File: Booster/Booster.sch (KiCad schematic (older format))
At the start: 0 parts

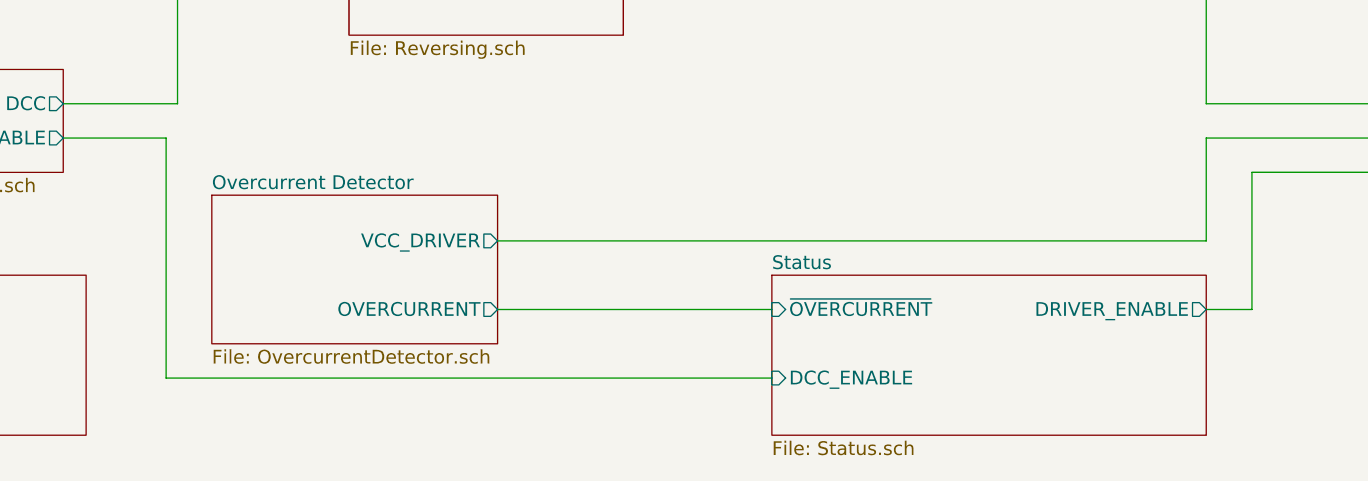
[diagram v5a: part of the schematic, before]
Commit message: Added 555 timer to control overcurrent release delay. Simpler to control as turning the power off cleared the overflow before the capacitor controlling the release delay was fully cleared. The LM339 is still doing the detect delay.
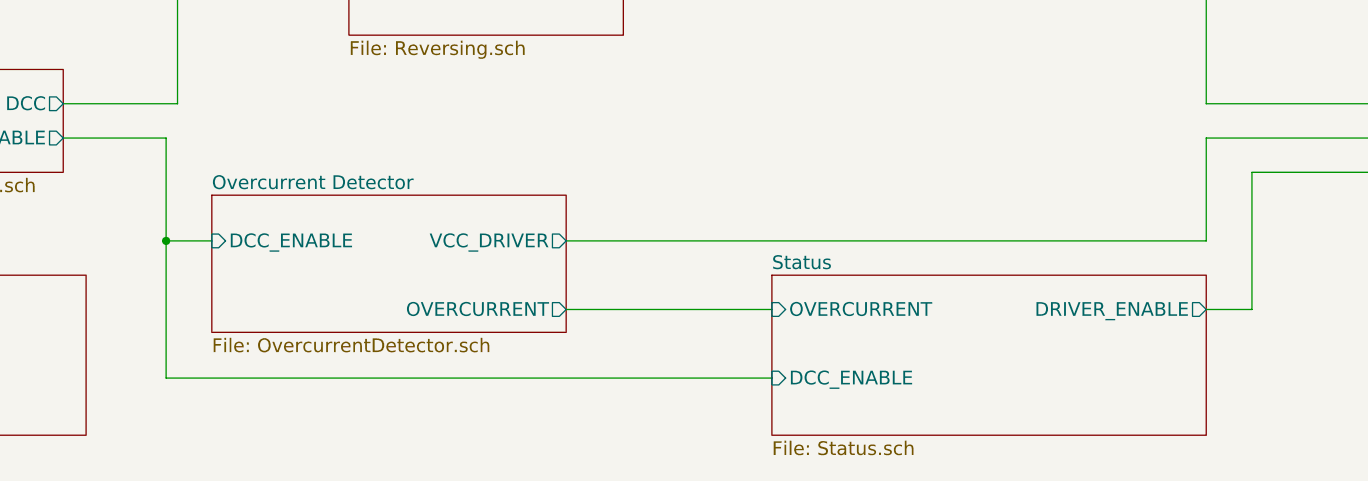
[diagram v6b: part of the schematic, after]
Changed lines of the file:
@@
 $EndSheet
 $Sheet
-S 2850 4500 1250 650
+S 2850 4500 1550 600
 U 59ECA16F
 F0 "Overcurrent Detector" 60
 F1 "OvercurrentDetector.sch" 60
-F2 "VCC_DRIVER" O R 4100 4700 60
-F3 "OVERCURRENT" O R 4100 5000 60
+F2 "VCC_DRIVER" O R 4400 4700 60
+F3 "OVERCURRENT" O R 4400 5000 60
+F4 "DCC_ENABLE" I L 2850 4700 60
 $EndSheet
 $Sheet
@@
 F1 "Status.sch" 60
 F2 "DCC_ENABLE" I L 5300 5300 60
-F3 "~OVERCURRENT" I L 5300 5000 60
-F4 "DRIVER_ENABLE" O R 7200 5000 60
+F3 "DRIVER_ENABLE" O R 7200 5000 60
+F4 "OVERCURRENT" I L 5300 5000 60
 $EndSheet
 Wire Wire Line
-	4100 4700 7200 4700
+	4400 4700 7200 4700
 Wire Wire Line
 	7200 4700 7200 4250
@@
 	2650 5300 5300 5300
 Wire Wire Line
-	4100 5000 5300 5000
+	4400 5000 5300 5000
 Wire Wire Line
 	7200 5000 7400 5000
@@
 Wire Wire Line
 	7400 4400 8550 4400
+Wire Wire Line
+	2850 4700 2650 4700
+Connection ~ 2650 4700
 $EndSCHEMATC

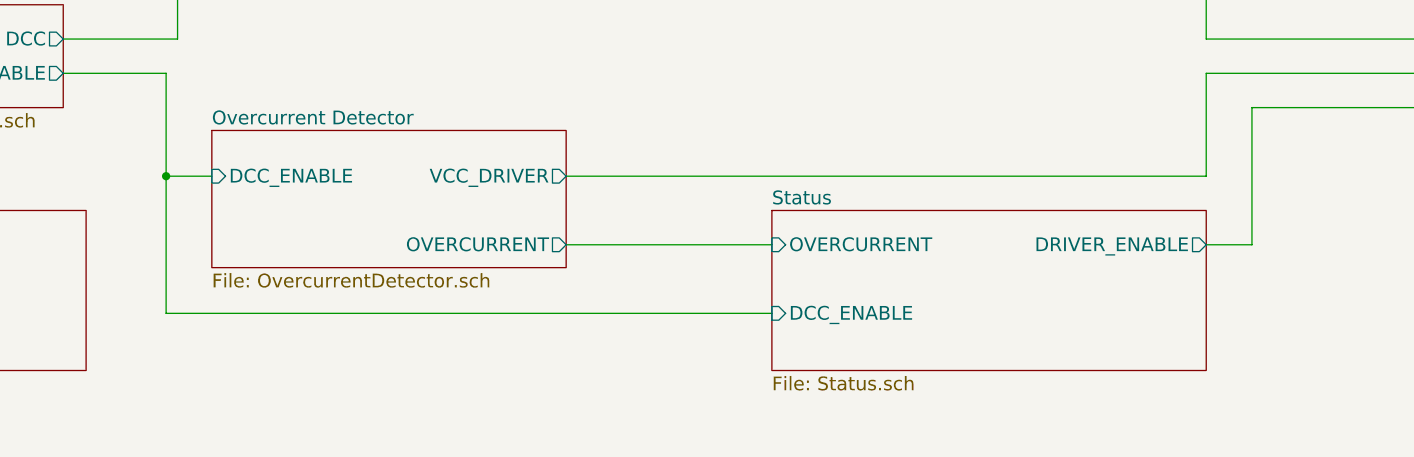
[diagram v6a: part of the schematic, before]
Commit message: Reset overcurrent timeout now linked to the master switch, not the input signal.
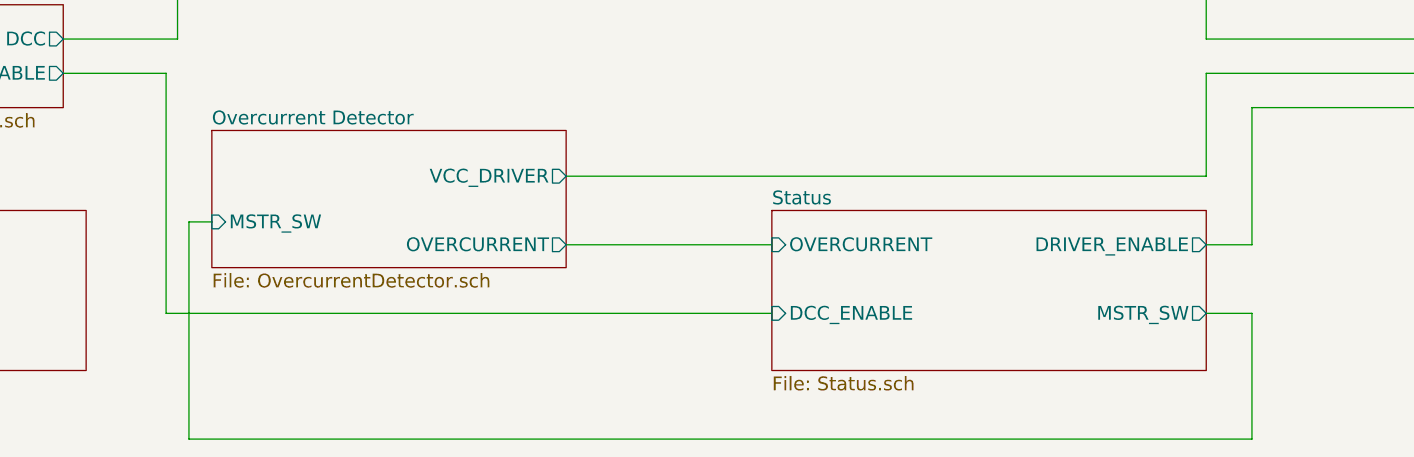
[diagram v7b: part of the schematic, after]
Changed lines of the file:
@@
 F2 "VCC_DRIVER" O R 4400 4700 60
 F3 "OVERCURRENT" O R 4400 5000 60
-F4 "DCC_ENABLE" I L 2850 4700 60
+F4 "MSTR_SW" I L 2850 4900 60
 $EndSheet
 $Sheet
@@
 F3 "DRIVER_ENABLE" O R 7200 5000 60
 F4 "OVERCURRENT" I L 5300 5000 60
+F5 "MSTR_SW" O R 7200 5300 60
 $EndSheet
 Wire Wire Line
@@
 	7400 4400 8550 4400
 Wire Wire Line
-	2850 4700 2650 4700
-Connection ~ 2650 4700
+	2850 4900 2750 4900
+Wire Wire Line
+	2750 4900 2750 5850
+Wire Wire Line
+	2750 5850 7400 5850
+Wire Wire Line
+	7200 5300 7400 5300
+Wire Wire Line
+	7400 5300 7400 5850
 $EndSCHEMATC

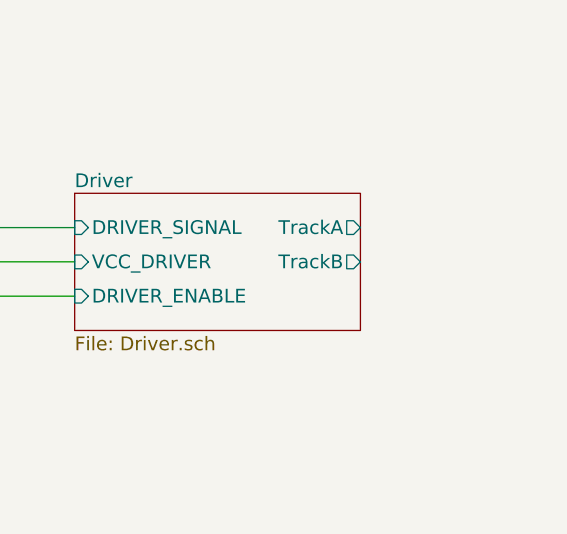
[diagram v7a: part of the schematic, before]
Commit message: Fixed missing connections.
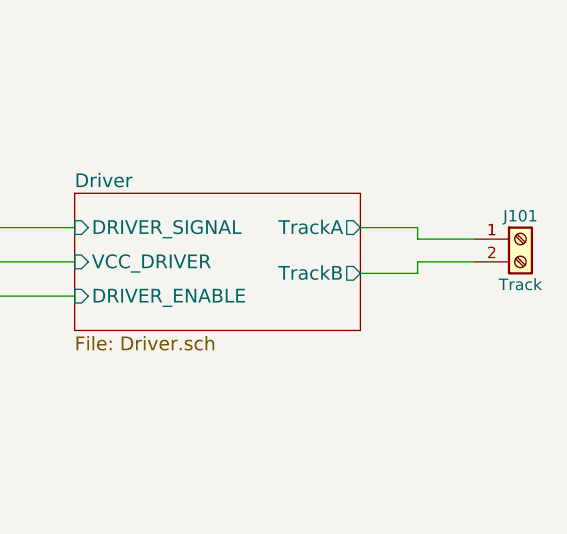
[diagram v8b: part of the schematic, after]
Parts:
- added J101: Track, symbol Screw_Terminal_01x02
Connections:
- net Driver/TrackA: now also J101.1 (Pin_1)
- net Driver/TrackB: now also J101.2 (Pin_2)
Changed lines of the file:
@@
 F1 "Driver.sch" 60
 F2 "TrackA" O R 9800 4100 60
-F3 "TrackB" O R 9800 4250 60
+F3 "TrackB" O R 9800 4300 60
 F4 "DRIVER_ENABLE" I L 8550 4400 60
 F5 "DRIVER_SIGNAL" I L 8550 4100 60
@@
 Wire Wire Line
 	7400 5300 7400 5850
+$Comp
+L Screw_Terminal_01x02 J101
+U 1 1 5A3994FE
+P 10500 4150
+F 0 "J101" H 10500 4250 50  0000 C CNN
+F 1 "Track" H 10500 3950 50  0000 C CNN
+F 2 "" H 10500 4150 50  0001 C CNN
+F 3 "" H 10500 4150 50  0001 C CNN
+	1    10500 4150
+	1    0    0    -1
+$EndComp
+Wire Wire Line
+	9800 4300 10050 4300
+Wire Wire Line
+	10050 4300 10050 4250
+Wire Wire Line
+	10050 4250 10300 4250
+Wire Wire Line
+	10300 4150 10050 4150
+Wire Wire Line
+	10050 4150 10050 4100
+Wire Wire Line
+	10050 4100 9800 4100
 $EndSCHEMATC
